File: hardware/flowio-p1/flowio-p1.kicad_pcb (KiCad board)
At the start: 4 copper layers, 100 x 80 mm, 164 parts, among them J1 USB-C PWR, J10 VALVE, J11 VALVE, J12 VALVE, J13 VALVE, J14 VALVE, J15 VALVE, J16 VALVE, J17 VALVE, J18 DEBUG-UART, J19 DEBUG-GPIO, J2 USB-C, J20 VALVE, J21 VALVE, J22 VALVE, J23 PUMP, J5 XH-4P, J6 XH-4P, J7 XH-4P, J8 XH-4P, J9 XH-4P, Q10 AO3400A, Q11 SS8050, Q12 SS8050, Q13 AO3400A, Q14 AO3400A, Q15 AO3400A, Q16 AO3400A, Q3 AO3400A, Q4 AO3400A, Q5 AO3400A, Q6 AO3400A, Q7 AO3400A, Q8 AO3400A, Q9 AO3400A, SW1 RST, SW2 BOOT, SW3 USER, U1 ESP32-S3-WROOM-1-N16R8, U2 TCA9548APWR, U3 TPS54331DR, U4 CH340K, U5 USBLC6-2SC6, U6 XGZP6897D, U7 USBLC6-2SC6

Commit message: feat(T4b): stage2/3 障碍模型真值化+同位铜去重 — DRC 0 错 (183→172 未连)
- zone 幂等守卫真正跳过 (只 print 不跳会让累积重跑重建 9 平面 → 10x zones_intersect)
- 焊盘障碍: 外接圆改朝向矩形半边长; 自定义 pad (J2.7 屏蔽腿 x4) GetSize 撒谎
  0.01x0.01 → 回落 GetBoundingBox 真值 1.9x1.1 (CC1 穿屏蔽腿 shorting 根因)
- 走线间距: 中心线 0.5 采 3 点 → 宽度感知 (新半宽+既有半宽+0.25) 双向密采
  0.3mm + 过孔入障 (LED_TX_K 距 0.8mm +3V3 逃逸线 0.073 间距根因)
- seg_ok 板界检查 [0.55,99.45]x[0.55,79.45] (J1 逃逸拐角曾布到 x=100.45 板外)
- 饥饿热焊盘第二批: R59/Q15/R23/Q16 GND 腿 FULL 实连 (stage2 走线割辐条)
- 存盘前同位铜去重 (过孔按网+坐标, 走线按网+层+无向端点): 幂等重跑防翻倍
- del_bad_via.py 升级铜柱环守门清扫 (SES 导入后兜底, case_geom 真值 PD2.8+环1.75)
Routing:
- net DRV_PUMP: track 0.00 -> 30.9 mm
- net DRV1: track 0.00 -> 19.9 mm
- net CC1: track 0.00 -> 12.3 mm
- net DRV_F: track 0.00 -> 9.02 mm
- net USB_DN: track 0.00 -> 8.55 mm
- net GATE_F: track 0.00 -> 7.20 mm
- net GATE_V: track 0.00 -> 6.86 mm
- net DRV8: track 0.00 -> 4.54 mm
- net DRV5: track 0.00 -> 4.54 mm

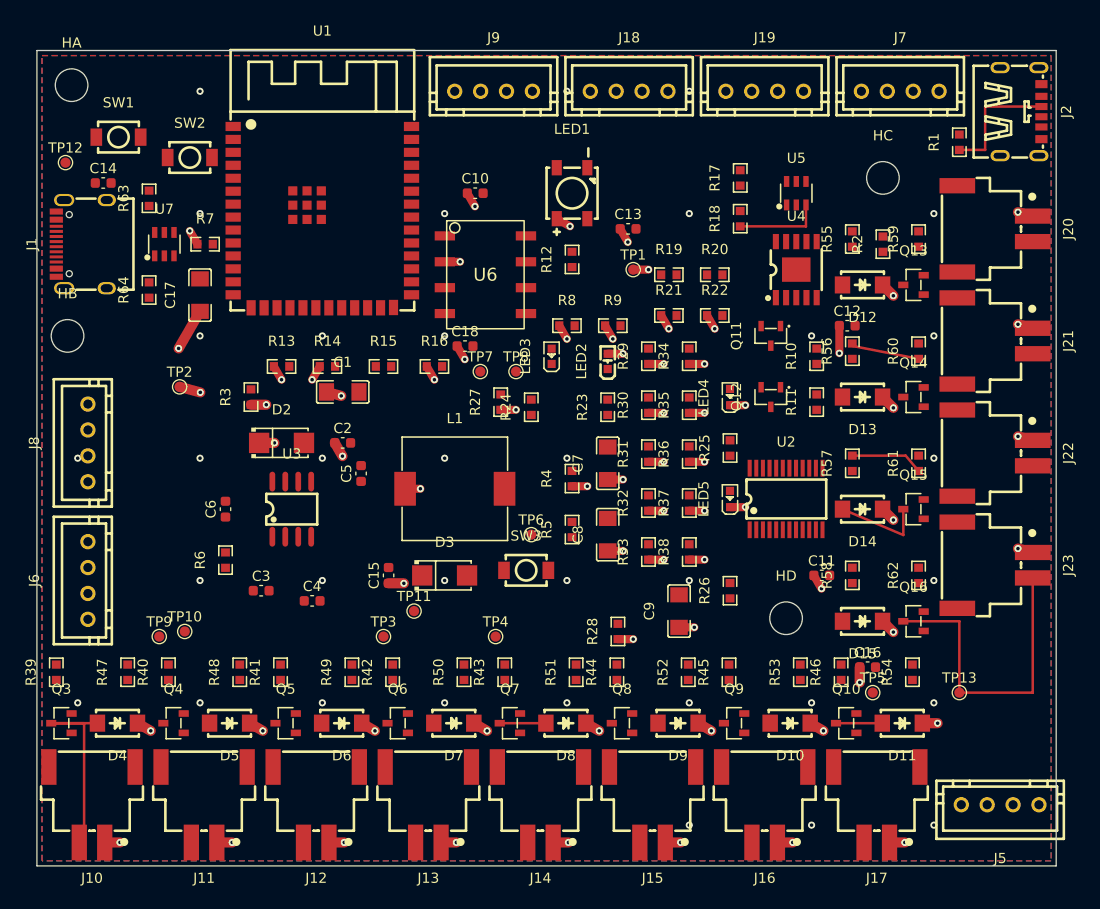
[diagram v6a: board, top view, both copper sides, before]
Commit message: feat(T4c): freerouting round4 + 阶段4 电源收尾 — DRC 0 错 (183→49 未连)
- freerouting v2.4.1 headless (jdk-25): -mp 200 -us hybrid -hr 1:1
  improvement_threshold=0.0 via_costs=80 + optimizer max_passes=3
  (实测 optimizer 5 轮 0 改进, 不设上限会跑满 200 轮 ≈5h)
- 扇出 388/390 SMD; 自动布线 110→6 未连; SES 117KB 导入: 1196 走线/266 过孔
- 阶段4 (独立路径提前退出, 不重跑 1-3):
  * J1 +5V 入口: 0.2 狗骨 x1 + 0.5 左缘总线 (与 freerouting 西逃逸网同节点并联),
    0.15 扇出短桩全数加宽 0.2 (netclass)
  * Z5NECK 颈桥平面 (6-17,32.5-38) prio6: Z5a-Z5b 2.5mm 共边 + freerouting
    In2 信号线 (S4_SDA/+3V3) 穿颈, 走线桥无窗 → 平面填充自动 carve
- CH_TX y19.78→19.82 (加宽后距 U4.6 RTS 0.18→0.22)
- 饥饿热焊盘第三批 x9 FULL 实连 (Q13/Q14/R24/R47/R64/U3.7/U2.1/U4.11/C16.2)
- 删 B4A9 右狗骨通道 x4 (与 freerouting CC1 拐线同位冲突)
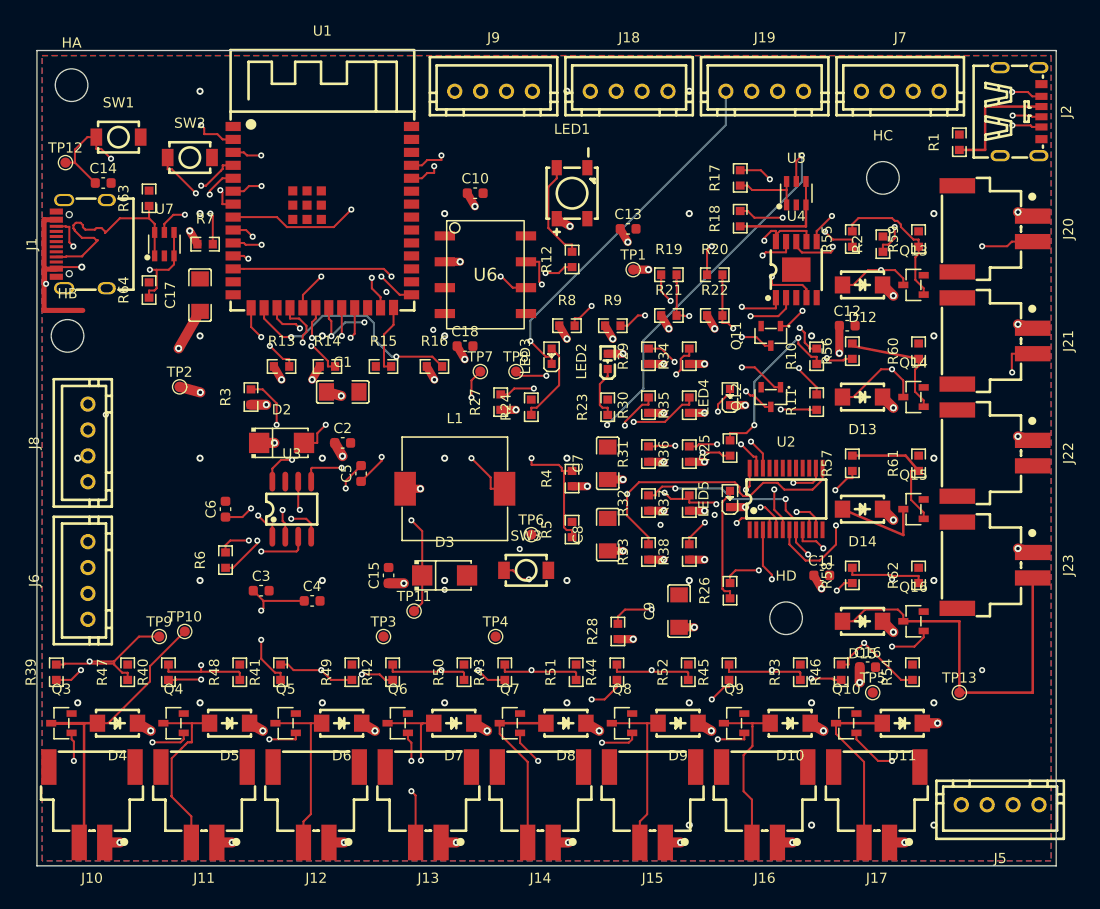
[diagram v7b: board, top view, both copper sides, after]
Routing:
- net BOOT: track 0.00 -> 131.1 mm, vias 0 -> 6
- net BTN_USER: track 0.00 -> 111.6 mm, vias 0 -> 3
- net S2_SCL: track 0.00 -> 109.3 mm, vias 0 -> 2
- net USB_VBUS: track 0.00 -> 99.8 mm, vias 0 -> 5
- net EN: track 0.00 -> 94.0 mm, vias 0 -> 4
- net I2C_SDA: track 0.00 -> 92.0 mm, vias 0 -> 5
- net S2_SDA: track 0.00 -> 90.6 mm, vias 0 -> 3
- net IO18: track 0.00 -> 82.7 mm, vias 0 -> 4
- net S4_SCL: track 0.00 -> 81.5 mm, vias 0 -> 3
- net +3V3: track 55.2 -> 136.1 mm, vias 36 -> 41
- net S4_SDA: track 0.00 -> 80.5 mm, vias 0 -> 2
- net I2C_SCL: track 0.00 -> 79.7 mm, vias 0 -> 5
- net S3_SCL: track 0.00 -> 76.3 mm, vias 0 -> 2
- net S3_SDA: track 0.00 -> 75.5 mm, vias 0 -> 3
- net IO21: track 0.00 -> 74.2 mm, vias 0 -> 3
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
